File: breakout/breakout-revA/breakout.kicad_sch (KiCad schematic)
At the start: 228 parts, among them J300 Breakout Connector, J301 Breakout Connector, P1 Conn_01x03, P2 Conn_01x03, P3 Conn_01x03, Q1 MMBT3906-7-F, Q10 MMBT3904-TP, Q11 MMBT3906-7-F, Q12 MMBT3904-TP, Q13 MMBT3906-7-F, Q14 MMBT3904-TP, Q15 MMBT3906-7-F, Q16 MMBT3904-TP, Q17 MMBT3906-7-F, Q18 MMBT3904-TP, Q19 MMBT3906-7-F, Q2 MMBT3906-7-F, Q20 MMBT3904-TP, Q21 MMBT3906-7-F, Q22 MMBT3904-TP, Q23 MMBT3904-TP, Q3 MMBT3906-7-F, Q4 MMBT3906-7-F, Q5 MMBT3906-7-F, Q6 MMBT3904-TP, Q7 MMBT3906-7-F, Q8 MMBT3904-TP, Q9 MMBT3906-7-F, SW1 A6SN-5104, SW2 PTS810 SJS 250 SMTR LFS, SW3 PTS810 SJS 250 SMTR LFS, SW4 PTS810 SJS 250 SMTR LFS

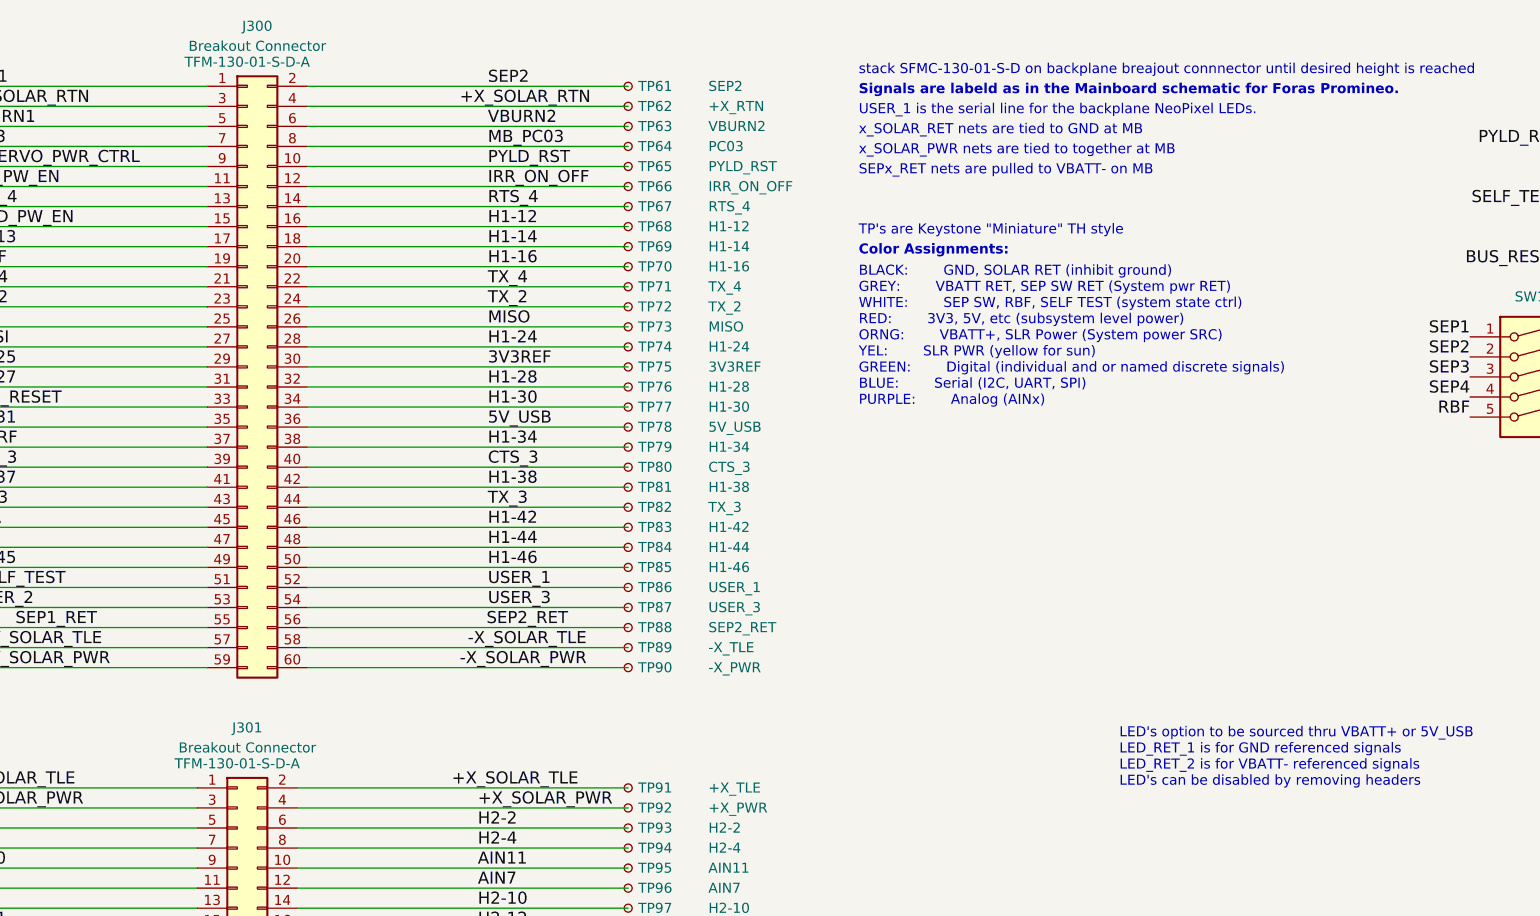
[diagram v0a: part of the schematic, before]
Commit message: updated silk screen, bom, and sub J301.
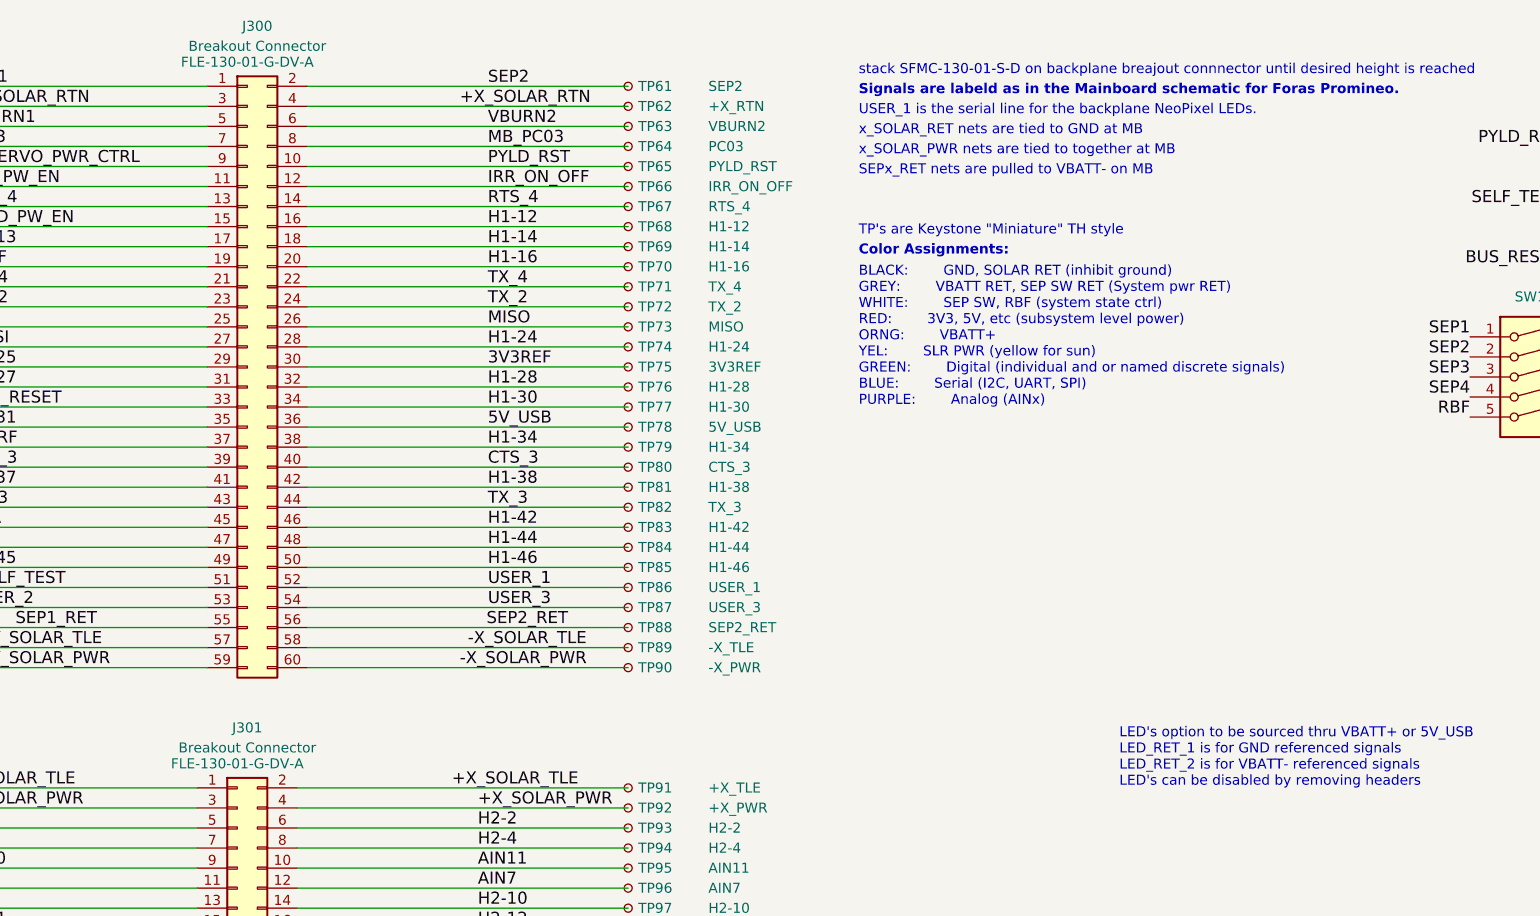
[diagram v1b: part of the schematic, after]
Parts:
- J300, J301: Manufacturer Part Number 1 TFM-130-01-S-D-A -> FLE-130-01-G-DV-A
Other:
- note added: "BLACK: GND, SOLAR RET (inhibit ground) GREY: VBATT RET, SEP SW RET (System pwr RET) WHITE: SEP SW, RBF (system state ctrl) RED: 3V3, 5V, etc (subsystem level power) ORNG: VBATT+ YEL: SLR PWR (yellow for sun) GREEN: Digital (individual and or named discrete signals) BLUE: Serial (I2C, UART, SPI) PURPLE: Analog (AINx)"
- note removed: "BLACK: GND, SOLAR RET (inhibit ground) GREY: VBATT RET, SEP SW RET (System pwr RET) WHITE: SEP SW, RBF, SELF TEST (system state ctrl) RED: 3V3, 5V, etc (subsystem level power) ORNG: VBATT+, SLR Power (System power SRC) YEL: SLR PWR (yellow for sun) GREEN: Digital (individual and or named discrete signals) BLUE: Serial (I2C, UART, SPI) PURPLE: Analog (AINx)"
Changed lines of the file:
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@@
     (effects (font (size 1.27 1.27)) (justify left bottom))
   )
-  (text "BLACK:		GND, SOLAR RET (inhibit ground)\nGREY:		VBATT RET, SEP SW RET (System pwr RET)\nWHITE:		SEP SW, RBF, SELF TEST (system state ctrl)\nRED:		3V3, 5V, etc (subsystem level power)\nORNG:		VBATT+, SLR Power (System power SRC)\nYEL:		SLR PWR (yellow for sun)\nGREEN:		Digital (individual and or named discrete signals)\nBLUE:		Serial (I2C, UART, SPI)\nPURPLE:		Analog (AINx)\n"
+  (text "BLACK:		GND, SOLAR RET (inhibit ground)\nGREY:		VBATT RET, SEP SW RET (System pwr RET)\nWHITE:		SEP SW, RBF (system state ctrl)\nRED:		3V3, 5V, etc (subsystem level power)\nORNG:		VBATT+\nYEL:		SLR PWR (yellow for sun)\nGREEN:		Digital (individual and or named discrete signals)\nBLUE:		Serial (I2C, UART, SPI)\nPURPLE:		Analog (AINx)\n"
     (at 177.8 63.5 0)
     (effects (font (size 1.27 1.27)) (justify left bottom))
@@
       (effects (font (size 1.27 1.27)) hide)
     )
-    (property "Datasheet" "TFM-130-01-S-D-A" (id 3) (at 100.33 19.05 0)
+    (property "Datasheet" "FLE-130-01-G-DV-A" (id 3) (at 100.33 19.05 0)
       (effects (font (size 1.27 1.27)) (justify top))
     )
-    (property "Manufacturer Part Number 1" "TFM-130-01-S-D-A" (id 4) (at 100.33 58.42 0)
+    (property "Manufacturer Part Number 1" "FLE-130-01-G-DV-A" (id 4) (at 100.33 58.42 0)
       (effects (font (size 1.27 1.27)) hide)
     )
@@
       (effects (font (size 1.27 1.27)) hide)
     )
-    (property "Datasheet" "TFM-130-01-S-D-A" (id 3) (at 99.06 107.95 0)
+    (property "Datasheet" "FLE-130-01-G-DV-A" (id 3) (at 99.06 107.95 0)
       (effects (font (size 1.27 1.27)) (justify top))
     )
-    (property "Manufacturer Part Number 1" "TFM-130-01-S-D-A" (id 4) (at 99.06 147.32 0)
+    (property "Manufacturer Part Number 1" "FLE-130-01-G-DV-A" (id 4) (at 99.06 147.32 0)
       (effects (font (size 1.27 1.27)) hide)
     )
